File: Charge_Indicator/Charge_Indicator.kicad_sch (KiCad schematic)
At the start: 76 parts, among them J1 PZ254-2-02-S, J2 1711725, J3 1711725, J4 PZ254-2-02-S, M1 M3, M2 M3, M3 M3, M4 M3, Q1 BSS84-7-F, Q2 2N7002P,215, SW1 SSSS811101, U1 BQ34Z100-R2, U2 SGM61410XN6G_TR, U3 INA226, U4 SN74HC164PWR, U5 TPS7A2033PDBVR, U6 TLV271CW5-7

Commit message: Organizing.
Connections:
- net +5v: no longer C11.2 (1), R18.1
- net ENABLE: no longer U1.2 (VEN)
- net at U1.7 (REG25): now also C11.2 (1), R18.1
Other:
- note added: "Notes: R18 is now a Thermistor. R4 is now a 0.01Ω Pulse Resistor R26 is now a 0.005Ω Pulse Resistor"
- note added: "Notes: REG25 even though unused needs to be decoupled to VSS Or else bad stuff happens"
- moved on the sheet: R17
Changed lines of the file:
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@@
 		)
 	)
+	(text "Notes:	\nREG25 even though \nunused needs to be \ndecoupled to VSS\n  Or else bad stuff happens"
+		(exclude_from_sim no)
+		(at 63.246 137.414 0)
+		(effects
+			(font
+				(size 1.27 1.27)
+				(color 0 16 255 1)
+			)
+			(justify left)
+		)
+	)
 	(text "3.3V Fully Regulated"
 		(exclude_from_sim no)
@@
 		)
 	)
+	(text "Notes:	\nR18 is now a Thermistor.\nR4 is now a 0.01Ω Pulse Resistor\nR26 is now a 0.005Ω Pulse Resistor"
+		(exclude_from_sim no)
+		(at 90.17 130.048 0)
+		(effects
+			(font
+				(size 1.27 1.27)
+				(color 0 16 255 1)
+			)
+			(justify left)
+		)
+	)
 	(text "Peripheral Connections Block"
 		(exclude_from_sim no)
@@
 	)
 	(junction
-		(at 34.29 92.71)
-		(diameter 0)
-		(color 0 0 0 0)
-	)
-	(junction
 		(at 46.99 160.02)
 		(diameter 0)
@@
 	)
 	(junction
-		(at 74.93 123.19)
+		(at 24.13 93.98)
 		(diameter 0)
 		(color 0 0 0 0)
 	)
 	(junction
-		(at 24.13 93.98)
+		(at 74.93 123.19)
 		(diameter 0)
 		(color 0 0 0 0)
@@
 	)
 	(junction
-		(at 64.77 123.19)
-		(diameter 0)
-		(color 0 0 0 0)
-	)
-	(junction
 		(at 107.95 158.75)
 		(diameter 0)
@@
 	(wire
 		(pts
-			(xy 34.29 92.71) (xy 39.37 92.71)
-		)
-		(stroke
-			(width 0)
-			(type default)
-		)
-	)
-	(wire
-		(pts
 			(xy 24.13 93.98) (xy 24.13 95.25)
 		)
@@
 	(wire
 		(pts
-			(xy 27.94 92.71) (xy 34.29 92.71)
+			(xy 27.94 130.81) (xy 39.37 130.81)
 		)
 		(stroke
@@
 	(wire
 		(pts
-			(xy 34.29 130.81) (xy 34.29 92.71)
-		)
-		(stroke
-			(width 0)
-			(type default)
-		)
-	)
-	(wire
-		(pts
 			(xy 60.96 48.26) (xy 60.96 54.61)
 		)
@@
 	(wire
 		(pts
-			(xy 17.78 87.63) (xy 17.78 86.36)
+			(xy 26.67 135.89) (xy 22.86 135.89)
 		)
 		(stroke
@@
 	(wire
 		(pts
-			(xy 48.26 180.34) (xy 49.53 180.34)
+			(xy 17.78 87.63) (xy 17.78 86.36)
 		)
 		(stroke
@@
 	(wire
 		(pts
-			(xy 64.77 123.19) (xy 74.93 123.19)
+			(xy 48.26 180.34) (xy 49.53 180.34)
 		)
 		(stroke
@@
 	(wire
 		(pts
+			(xy 39.37 123.19) (xy 74.93 123.19)
+		)
+		(stroke
+			(width 0)
+			(type default)
+		)
+	)
+	(wire
+		(pts
 			(xy 116.84 25.4) (xy 124.46 25.4)
 		)
@@
 	(wire
 		(pts
-			(xy 39.37 130.81) (xy 34.29 130.81)
-		)
-		(stroke
-			(width 0)
-			(type default)
-		)
-	)
-	(wire
-		(pts
 			(xy 53.34 182.88) (xy 48.26 182.88)
 		)
@@
 	(wire
 		(pts
-			(xy 36.83 123.19) (xy 64.77 123.19)
-		)
-		(stroke
-			(width 0)
-			(type default)
-		)
-	)
-	(wire
-		(pts
 			(xy 88.9 92.71) (xy 97.79 92.71)
 		)
@@
 	(wire
 		(pts
-			(xy 64.77 123.19) (xy 64.77 125.73)
-		)
-		(stroke
-			(width 0)
-			(type default)
-		)
-	)
-	(wire
-		(pts
 			(xy 107.95 147.32) (xy 113.03 147.32)
 		)
@@
 	(wire
 		(pts
-			(xy 179.07 156.21) (xy 201.93 156.21)
+			(xy 39.37 118.11) (xy 39.37 123.19)
 		)
 		(stroke
@@
 	(wire
 		(pts
-			(xy 97.79 92.71) (xy 97.79 100.33)
+			(xy 179.07 156.21) (xy 201.93 156.21)
 		)
 		(stroke
@@
 	(wire
 		(pts
-			(xy 176.53 30.48) (xy 176.53 27.94)
+			(xy 97.79 92.71) (xy 97.79 100.33)
 		)
 		(stroke
@@
 	(wire
 		(pts
-			(xy 161.29 109.22) (xy 168.91 109.22)
+			(xy 176.53 30.48) (xy 176.53 27.94)
 		)
 		(stroke
@@
 	(wire
 		(pts
-			(xy 36.83 125.73) (xy 36.83 135.89)
+			(xy 161.29 109.22) (xy 168.91 109.22)
 		)
 		(stroke
@@
 	(wire
 		(pts
-			(xy 60.96 48.26) (xy 72.39 48.26)
+			(xy 36.83 135.89) (xy 39.37 135.89)
 		)
 		(stroke
@@
 	(wire
 		(pts
-			(xy 99.06 182.88) (xy 96.52 182.88)
+			(xy 60.96 48.26) (xy 72.39 48.26)
 		)
 		(stroke
@@
 	(wire
 		(pts
-			(xy 54.61 125.73) (xy 36.83 125.73)
+			(xy 99.06 182.88) (xy 96.52 182.88)
 		)
 		(stroke
@@
 	(wire
 		(pts
-			(xy 36.83 135.89) (xy 39.37 135.89)
-		)
-		(stroke
-			(width 0)
-			(type default)
-		)
-	)
-	(wire
-		(pts
 			(xy 72.39 27.94) (xy 67.31 27.94)
 		)
@@
 		)
 	)
+	(label "VSS"
+		(at 83.82 118.11 0)
+		(effects
+			(font
+				(size 1.27 1.27)
+			)
+			(justify left bottom)
+		)
+	)
 	(label "Battery_Input_25.6V"
 		(at 25.4 34.29 0)
@@
 	)
 	(label "ENABLE"
-		(at 27.94 92.71 0)
+		(at 27.94 130.81 0)
 		(effects
 			(font
@@
 		(lib_name "R_2P_6")
 		(lib_id "wn__wavenumber:R_2P")
-		(at 54.61 125.73 0)
+		(at 36.83 135.89 180)
 		(unit 1)
 		(exclude_from_sim no)
@@
 		(dnp no)
 		(property "Reference" "R17"
-			(at 64.516 129.54 0)
+			(at 29.464 133.858 0)
 			(effects
 				(font
@@
 		)
 		(property "Value" "1kΩ"
-			(at 63.246 127.254 0)
+			(at 34.29 134.112 0)
 			(effects
 				(font
@@
 		)
 		(property "Footprint" "wavenumber:R0603_0.55MM_HD"
-			(at 54.61 125.73 0)
+			(at 36.83 135.89 0)
 			(effects
 				(font
@@
 		)
 		(property "Datasheet" ""
-			(at 54.61 125.73 0)
+			(at 36.83 135.89 0)
 			(effects
 				(font
@@
 		)
 		(property "Description" "RES 1K OHM 1/10W 1% 0603 SMD"
-			(at 54.61 125.73 0)
+			(at 36.83 135.89 0)
 			(effects
 				(font
@@
 		)
 		(property "Internal Part Number" ""
-			(at 54.61 125.73 0)
+			(at 36.83 135.89 0)
 			(effects
 				(font
@@
 		)
 		(property "Manufacturer" "Panasonic Electronic Components"
-			(at 54.61 125.73 0)
+			(at 36.83 135.89 0)
 			(effects
 				(font
@@
 		)
 		(property "Manufacturer Part Number" "ERJ-3EKF1001V"
-			(at 54.61 125.73 0)
+			(at 36.83 135.89 0)
 			(effects
 				(font
@@
 		)
 		(property "cad-reference" "ERJ-3EKF1001V"
-			(at 54.61 125.73 0)
+			(at 36.83 135.89 0)
 			(effects
 				(font
@@
 		)
 		(property "flags" ""
-			(at 54.61 125.73 0)
+			(at 36.83 135.89 0)
 			(effects
 				(font
@@
 	(symbol
 		(lib_id "wn_pwr:+5v")
-		(at 36.83 123.19 0)
+		(at 22.86 135.89 0)
 		(unit 1)
 		(exclude_from_sim no)
@@
 		(fields_autoplaced yes)
 		(property "Reference" "#PWR034"
-			(at 36.83 119.39 0)
+			(at 22.86 132.09 0)
 			(do_not_autoplace yes)
 			(effects
@@
 		)
 		(property "Value" "+5v"
-			(at 36.83 119.39 0)
+			(at 22.86 132.09 0)
 			(do_not_autoplace yes)
 			(effects
@@
 		)
 		(property "Footprint" ""
-			(at 36.83 123.19 0)
+			(at 22.86 135.89 0)
 			(effects
 				(font
@@
 		)
 		(property "Datasheet" ""
-			(at 36.83 123.19 0)
+			(at 22.86 135.89 0)
 			(effects
 				(font
@@
 		)
 		(property "Description" "Power symbol creates a global label with name \"+5v\" , 5V power rail"
-			(at 37.592 113.538 0)
+			(at 23.622 126.238 0)
 			(effects
 				(font

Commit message: Changes to the PCB for REV 3
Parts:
- removed R18: 10kΩ, wavenumber:R1206_0.70MM_HD, symbol wn__wavenumber:R_2P
- added R31: 1kΩ, wavenumber:R0603_0.55MM_HD, symbol wn__wavenumber:R_2P
- R17: value 1kΩ -> 10kΩ; Manufacturer Part Number ERJ-3EKF1001V -> ERJ-3EKF1002V; cad-reference ERJ-3EKF1001V -> ERJ-3EKF1002V
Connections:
- net +5v: now also SW1.2; no longer R17.2
- net at R17.1: now also C11.2 (1), U1.7 (REG25), R31.1; no longer SW1.2
- net at U1.11 (P6/TS): now also R17.2
- net at U1.2 (VEN): now also R31.2
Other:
- note added: "Notes: R18 is now a Thermistor. R4 is now a 0.01Ω Pulse Resistor R26 is now a 0.005Ω Pulse Resistor [Components not created yet]"
- note added: "Star Ground"
- note removed: "Notes: R18 is now a Thermistor. R4 is now a 0.01Ω Pulse Resistor R26 is now a 0.005Ω Pulse Resistor"
- note removed: "Notes: REG25 even though unused needs to be decoupled to VSS Or else bad stuff happens"
- moved on the sheet: C11

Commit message: Fixing Net issue
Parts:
- added NT1: NetTie_StarGround, autonav_fp:NetTie_StarGround, symbol NetTie_StarGround:NetTie_StarGround
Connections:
- net AGND: now also NT1.1; no longer C1.2 (1), C12.2 (1), C13.2 (1), C3.2 (1), C5.2 (1), C6.1, C7.2 (1), C8.2 (1), D7.1 (A), D8.1 (A), D9.1 (A), J1.3, J2.1, M1.1, M2.1, M3.1, M4.1, Q2.2 (S), R19.2, R20.1, R22.2, R26.2, R3.2, SW1.M, U2.2 (GND), U3.1 (A1), U3.2 (A0), U3.7 (GND), U4.7 (GND), U5.2 (GND), U6.2 (GND)
- new net GND: C1.2 (1), C12.2 (1), C13.2 (1), C3.2 (1), C5.2 (1), C6.1, C7.2 (1), C8.2 (1), D7.1 (A), D8.1 (A), D9.1 (A), J1.3, J2.1, M1.1, M2.1, M3.1, M4.1, NT1.2, Q2.2 (S), R19.2, R20.1, R22.2, R26.2, R3.2, SW1.M, U2.2 (GND), U3.1 (A1), U3.2 (A0), U3.7 (GND), U4.7 (GND), U5.2 (GND), U6.2 (GND)
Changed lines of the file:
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@@
 	(text "Star Ground"
 		(exclude_from_sim no)
-		(at 117.094 116.078 0)
+		(at 117.094 112.268 0)
 		(effects
 			(font
@@
 	(wire
 		(pts
+			(xy 116.84 109.22) (xy 116.84 116.84)
+		)
+		(stroke
+			(width 0)
+			(type default)
+		)
+	)
+	(wire
+		(pts
 			(xy 179.07 157.48) (xy 179.07 156.21)
 		)
@@
 	(wire
 		(pts
+			(xy 127 116.84) (xy 127 109.22)
+		)
+		(stroke
+			(width 0)
+			(type default)
+		)
+	)
+	(wire
+		(pts
 			(xy 60.96 57.15) (xy 66.04 57.15)
 		)
@@
 	(wire
 		(pts
+			(xy 125.73 116.84) (xy 127 116.84)
+		)
+		(stroke
+			(width 0)
+			(type default)
+		)
+	)
+	(wire
+		(pts
+			(xy 118.11 116.84) (xy 116.84 116.84)
+		)
+		(stroke
+			(width 0)
+			(type default)
+		)
+	)
+	(wire
+		(pts
 			(xy 39.37 124.46) (xy 74.93 124.46)
 		)
@@
 	(wire
 		(pts
-			(xy 118.11 116.84) (xy 125.73 116.84)
-		)
-		(stroke
-			(width 0)
-			(type default)
-		)
-	)
-	(wire
-		(pts
 			(xy 48.26 187.96) (xy 49.53 187.96)
 		)
@@
 					(unit 1)
 				)
+			)
+		)
+	)
+	(symbol
+		(lib_id "NetTie_StarGround:NetTie_StarGround")
+		(at 121.92 109.22 0)
+		(unit 1)
+		(exclude_from_sim yes)
+		(in_bom no)
+		(on_board yes)
+		(dnp no)
+		(fields_autoplaced yes)
+		(property "Reference" "NT1"
+			(at 121.92 104.14 0)
+			(effects
+				(font
+					(size 1.27 1.27)
+				)
+			)
+		)
+		(property "Value" "NetTie_StarGround"
+			(at 121.92 106.68 0)
+			(effects
+				(font
+					(size 1.27 1.27)
+				)
+			)
+		)
+		(property "Footprint" "autonav_fp:NetTie_StarGround"
+			(at 121.92 109.22 0)
+			(effects
+				(font
+					(size 1.27 1.27)
+				)
+				(hide yes)
+			)
+		)
+		(property "Datasheet" ""
+			(at 121.92 109.22 0)
+			(effects
+				(font
+					(size 1.27 1.27)
+				)
+				(hide yes)
+			)
+		)
+		(property "Description" "Net tie for star ground — joins two ground nets at a single point"
+			(at 121.92 109.22 0)
+			(effects
+				(font
+					(size 1.27 1.27)
+				)
+				(hide yes)
+			)
+		)
+		(pin "2"
+		)
+		(pin "1"
+		)
+		(instances
+			(project ""
+				(path "/ce5a45ab-8fc2-45f1-907f-8e7f414ac528"
+					(reference "NT1")
+					(unit 1)
+				)

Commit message: Swapping out resistors at the divider to protect the BQ chip
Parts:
- R22, R30: value 34.8kΩ -> 6.49kΩ; Manufacturer Part Number ERJ-3EKF3482V -> ERJ-3EKF6491V; cad-reference ERJ-3EKF3482V -> ERJ-3EKF6491V
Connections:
- net at D1.1 (A), Q1.1 (G), R28.1: now also R30.2; no longer R30.1
- net at Q2.3 (D): now also R30.1; no longer R30.2

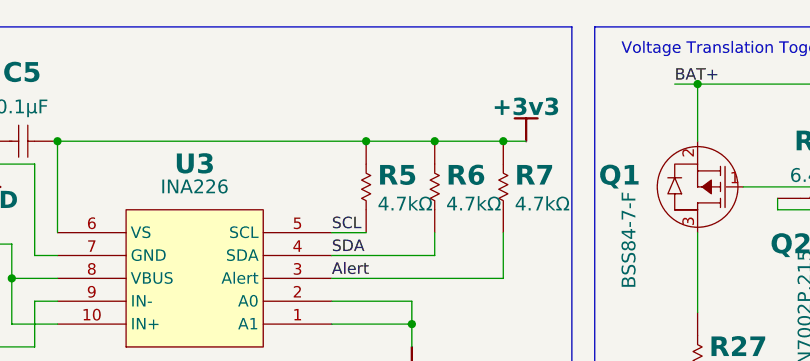
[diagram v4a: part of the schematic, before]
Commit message: BQ debugging and INA226 temp solution for coulomb counting
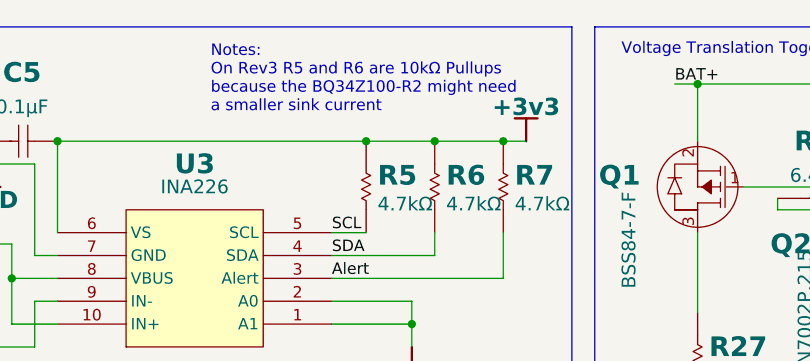
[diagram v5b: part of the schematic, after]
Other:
- note added: "Notes: On Rev3 R5 and R6 are 10kΩ Pullups because the BQ34Z100-R2 might need a smaller sink current"
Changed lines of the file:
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@@
+		)
+	)
+	(text "Notes:	\nOn Rev3 R5 and R6 are 10kΩ Pullups\nbecause the BQ34Z100-R2 might need\na smaller sink current"
+		(exclude_from_sim no)
+		(at 91.948 18.542 0)
+		(effects
+			(font
+				(size 1.27 1.27)
+				(color 0 16 255 1)
+			)
+			(justify left)
 		)
 	)

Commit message: Formatting for a report
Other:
- note added: "Front End Current, Voltage,and Power Sensor Block"
- note added: "Togglable Voltage Translation Block"
- note removed: "Front End Current, Voltage, Power Sensor Block"
- note removed: "Voltage Translation Togglable"
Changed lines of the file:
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@@
 		)
 	)
-	(text "Voltage Translation Togglable"
+	(text "Togglable Voltage Translation Block"
 		(exclude_from_sim no)
-		(at 150.622 15.24 0)
+		(at 165.354 15.748 0)
 		(effects
 			(font
-				(size 1.27 1.27)
+				(size 2.54 2.54)
+				(thickness 0.508)
+				(bold yes)
 				(color 0 16 255 1)
 			)
@@
 	(text "Peripheral Connections Block"
 		(exclude_from_sim no)
-		(at 27.178 171.958 0)
+		(at 38.354 173.736 0)
 		(effects
 			(font
-				(size 1.27 1.27)
+				(size 2.54 2.54)
+				(thickness 0.508)
+				(bold yes)
 				(color 0 16 255 1)
 			)
@@
 	(text "LED Driver Block"
 		(exclude_from_sim no)
-		(at 143.002 77.724 0)
+		(at 150.114 79.502 0)
 		(effects
 			(font
-				(size 1.27 1.27)
+				(size 2.54 2.54)
+				(thickness 0.508)
+				(bold yes)
 				(color 0 16 255 1)
 			)
@@
 	(text "5V DC-DC Buck Block"
 		(exclude_from_sim no)
-		(at 144.526 131.826 0)
+		(at 153.67 132.842 0)
 		(effects
 			(font
-				(size 1.27 1.27)
+				(size 2.54 2.54)
+				(thickness 0.508)
+				(bold yes)
 				(color 0 16 255 1)
 			)
@@
 	(text "Battery Gauge Block"
 		(exclude_from_sim no)
-		(at 23.622 78.232 0)
+		(at 30.734 79.248 0)
 		(effects
 			(font
-				(size 1.27 1.27)
+				(size 2.54 2.54)
+				(thickness 0.508)
+				(bold yes)
 				(color 0 16 255 1)
 			)
@@
 		)
 	)
-	(text "Front End Current, Voltage, Power Sensor Block"
+	(text "Front End Current, Voltage,and\nPower Sensor Block"
 		(exclude_from_sim no)
-		(at 36.576 14.986 0)
+		(at 13.716 18.288 0)
 		(effects
 			(font
-				(size 1.27 1.27)
+				(size 2.54 2.54)
+				(thickness 0.508)
+				(bold yes)
 				(color 0 16 255 1)
 			)
+			(justify left)
 		)
 	)
 	(text "3.3V DC-DC Regulator Block"
 		(exclude_from_sim no)
-		(at 95.758 169.418 0)
+		(at 105.918 170.688 0)
 		(effects
 			(font
-				(size 1.27 1.27)
+				(size 2.54 2.54)
+				(thickness 0.508)
+				(bold yes)
 				(color 0 16 255 1)
 			)
@@
 		(on_board yes)
 		(dnp no)
-		(fields_autoplaced yes)
 		(property "Reference" "U2"
-			(at 162.56 132.08 0)
+			(at 162.814 159.512 0)
 			(effects
 				(font
@@
 		)
 		(property "Value" "SGM61410XN6G_TR"
-			(at 162.56 134.62 0)
+			(at 162.814 162.56 0)
 			(effects
 				(font
